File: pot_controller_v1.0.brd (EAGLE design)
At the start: 91.1 x 63.2 mm, 30 parts, among them IC10 4051D, IC11 4051D, IC13 4051D, IC2 4051D, IC3 4520D, IC4 4051D, IC5 4051D, IC6 4051D, IC7 4051D, IC8 4051D

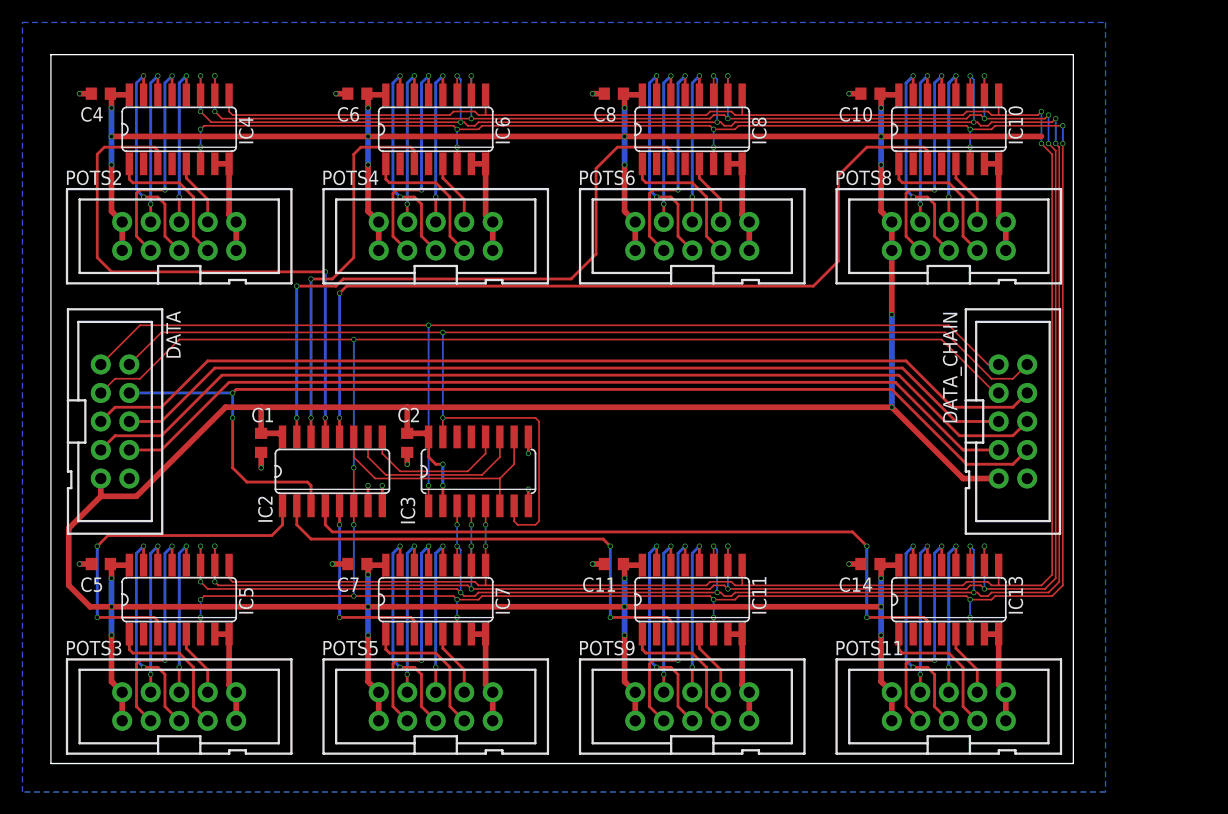
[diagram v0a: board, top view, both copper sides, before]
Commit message: Fixed routing except for possible inhibit-removal
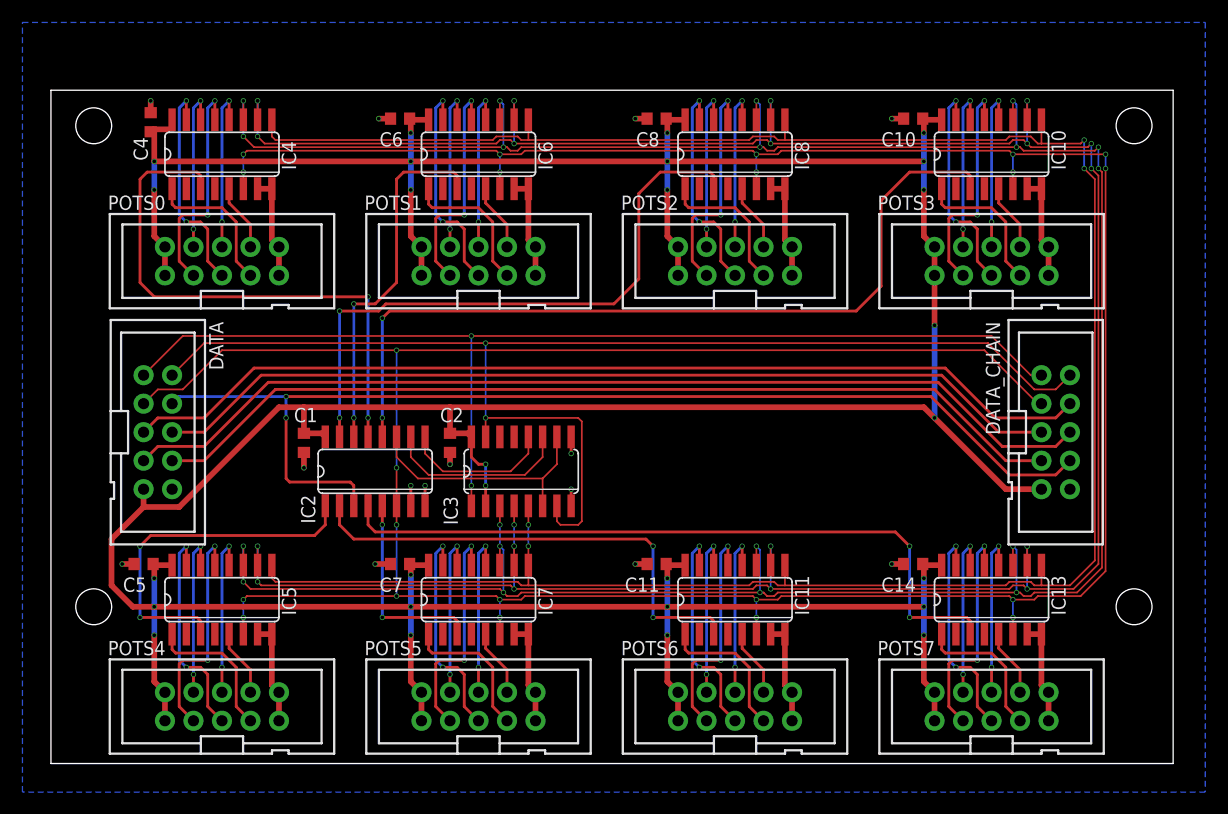
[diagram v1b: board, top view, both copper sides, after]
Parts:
- removed POTS11, POTS8, POTS9: CONN-IDC-10PS, joakim:CONN-IDC10P-S
- added POTS0, POTS1, POTS7: CONN-IDC-10PS, joakim:CONN-IDC10P-S
- moved POTS3 82.6 mm to (83.8, 44.8)
- moved POTS2 49.6 mm to (61.0, 44.8)
- moved POTS4 46.0 mm to (15.2, 5.08)
- moved POTS6 42.1 mm to (61.0, 5.08)
- moved C4 5.12 mm to (8.89, 57.1), turned to 90 degrees
- moved IC6 4.41 mm to (38.1, 54.3)
- moved IC8 4.41 mm to (61.0, 54.3)
- moved IC4 4.41 mm to (15.2, 54.3)
- moved C8 4.41 mm to (54.0, 57.5)
- moved C6 4.41 mm to (31.1, 57.5)
- moved IC10 4.41 mm to (83.8, 54.3)
- moved C10 4.41 mm to (76.8, 57.5)
- moved DATA_CHAIN 3.93 mm to (89.5, 29.5)
- moved DATA 3.93 mm to (9.53, 29.5)
- moved C11 3.81 mm to (54.0, 17.8)
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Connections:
- net +5V: now also POTS0.1, POTS0.2, POTS1.1, POTS1.2, POTS7.1, POTS7.2; no longer POTS11.1, POTS11.2, POTS8.1, POTS8.2, POTS9.1, POTS9.2
- net GND: now also POTS0.10, POTS0.9, POTS1.10, POTS1.9, POTS7.10, POTS7.9; no longer POTS11.10, POTS11.9, POTS8.10, POTS8.9, POTS9.10, POTS9.9
- net POT0: now also POTS0.3; no longer POTS2.3
- net POT1: now also POTS0.4; no longer POTS2.4
- net POT10: now also POTS1.7; no longer POTS4.7
- net POT11: now also POTS1.8; no longer POTS4.8
- net POT12: now also POTS2.3; no longer POTS6.3
- net POT13: now also POTS2.4; no longer POTS6.4
- net POT14: now also POTS2.5; no longer POTS6.5
- net POT15: now also POTS2.6; no longer POTS6.6
- net POT16: now also POTS2.7; no longer POTS6.7
- net POT17: now also POTS2.8; no longer POTS6.8
- net POT18: now also POTS3.3; no longer POTS8.3
- net POT19: now also POTS3.4; no longer POTS8.4
- net POT2: now also POTS0.5; no longer POTS2.5
- net POT20: now also POTS3.5; no longer POTS8.5
- net POT21: now also POTS3.6; no longer POTS8.6
- net POT22: now also POTS3.7; no longer POTS8.7
- net POT23: now also POTS3.8; no longer POTS8.8
- net POT24: now also POTS4.3; no longer POTS3.3
- net POT25: now also POTS4.4; no longer POTS3.4
- net POT26: now also POTS4.5; no longer POTS3.5
- net POT27: now also POTS4.6; no longer POTS3.6
- net POT28: now also POTS4.7; no longer POTS3.7
- net POT29: now also POTS4.8; no longer POTS3.8
- net POT3: now also POTS0.6; no longer POTS2.6
- net POT36: now also POTS6.3; no longer POTS9.3
- net POT37: now also POTS6.4; no longer POTS9.4
- net POT38: now also POTS6.5; no longer POTS9.5
- net POT39: now also POTS6.6; no longer POTS9.6
- net POT4: now also POTS0.7; no longer POTS2.7
- net POT40: now also POTS6.7; no longer POTS9.7
- net POT41: now also POTS6.8; no longer POTS9.8
- net POT42: now also POTS7.3; no longer POTS11.3
- net POT43: now also POTS7.4; no longer POTS11.4
- net POT44: now also POTS7.5; no longer POTS11.5
- net POT45: now also POTS7.6; no longer POTS11.6
- net POT46: now also POTS7.7; no longer POTS11.7
- net POT47: now also POTS7.8; no longer POTS11.8
- net POT5: now also POTS0.8; no longer POTS2.8
- net POT6: now also POTS1.3; no longer POTS4.3
- net POT7: now also POTS1.4; no longer POTS4.4
- net POT8: now also POTS1.5; no longer POTS4.5
- net POT9: now also POTS1.6; no longer POTS4.6
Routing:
- net +5V: track 412.7 -> 397.2 mm, vias 28 -> 27
- net POT_INH: track 328.3 -> 323.9 mm
- net POT_A: track 246.0 -> 242.6 mm
- net POT_B: track 239.2 -> 236.3 mm
- net POT_C: track 208.4 -> 205.6 mm
- net ROW2: track 57.7 -> 55.4 mm
- net ROW3: track 76.3 -> 74.1 mm
- net ROW1: track 34.8 -> 32.6 mm
- net ROW0: track 51.7 -> 49.5 mm
- net CLK: track 99.0 -> 98.0 mm
- net RESET: track 114.2 -> 113.2 mm
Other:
- board size 91.1 x 63.2 mm -> 100 x 60 mm

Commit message: Added silk screen
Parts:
- added U$1: (no value), joakim:XONIK_LOGO_60
- renumbered DATA_CHAIN to CHAIN
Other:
- board text added: "+V"
- board text added: "0"
- board text added: "1"
- board text added: "2"
- board text added: "3"
- board text added: "4"
- board text added: "48ch potentiometer scanner v1.0"
- board text added: "4VOB"
- board text added: "5"
- board text added: "CLK"
- board text added: "G"
- board text added: "GND"
- board text added: "O1"
- board text added: "O2"
- board text added: "O3"
- board text added: "O4"
- board text added: "O5"
- board text added: "RST"
- board text added: "V+"

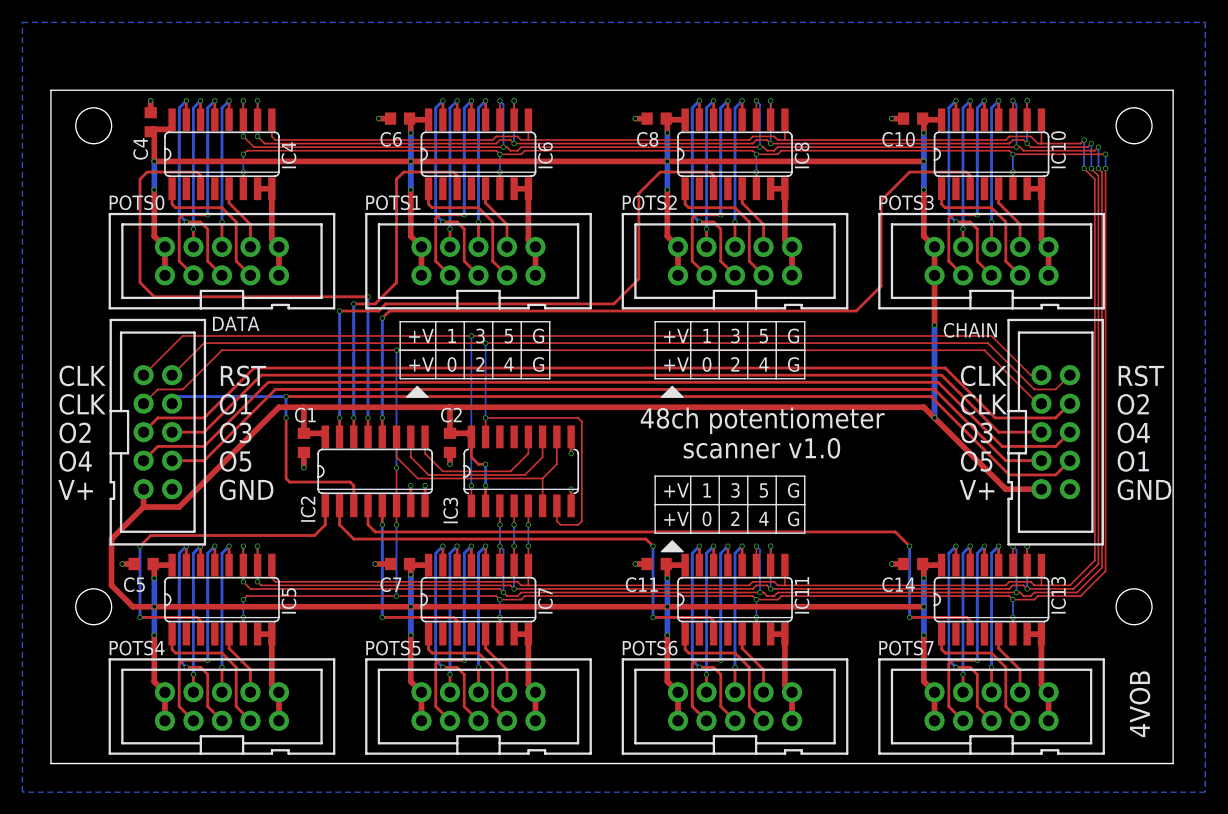
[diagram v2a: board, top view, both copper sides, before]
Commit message: Updated IDC connector
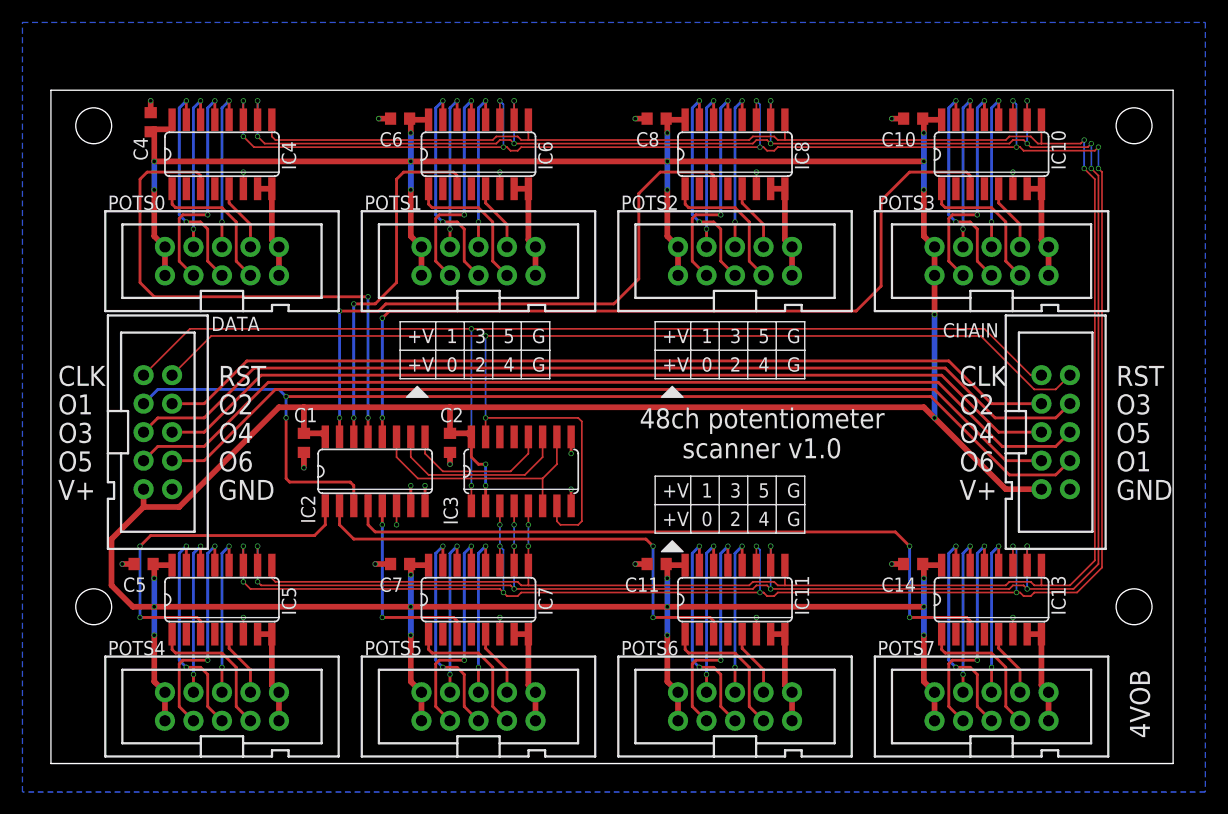
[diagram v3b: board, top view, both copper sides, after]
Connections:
- removed net POT_INH: CHAIN.3, DATA.3, IC10.6, IC11.6, IC13.6, IC2.6, IC4.6, IC5.6, IC6.6, IC7.6, IC8.6
- new net POT_VAL_CHAIN_5: CHAIN.7, DATA.8
- net GND: now also IC10.6, IC11.6, IC13.6, IC2.6, IC4.6, IC5.6, IC6.6, IC7.6, IC8.6
- net POT_VALUE: now also DATA.3; no longer DATA.4
- net POT_VAL_CHAIN_1: now also CHAIN.3, DATA.4; no longer CHAIN.4, DATA.5
- net POT_VAL_CHAIN_2: now also CHAIN.4, DATA.5; no longer CHAIN.5, DATA.6
- net POT_VAL_CHAIN_3: now also CHAIN.5, DATA.6; no longer CHAIN.6, DATA.7
- net POT_VAL_CHAIN_4: now also CHAIN.6, DATA.7; no longer CHAIN.7, DATA.8
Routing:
- net POT_INH: track 323.9 -> 0.00 mm, vias 22 -> 0
- net POT_VAL_CHAIN_5: track 0.00 -> 82.7 mm
- net GND: track 91.8 -> 105.4 mm, vias 14 -> 23
- net POT_VAL_CHAIN_3: track 88.3 -> 81.7 mm
- net POT_VAL_CHAIN_1: track 87.3 -> 80.6 mm
- net POT_VAL_CHAIN_2: track 81.7 -> 87.3 mm
- net POT_VAL_CHAIN_4: track 82.7 -> 88.3 mm
- net POT_VALUE: track 99.1 -> 102.2 mm
- net CLK: track 98.0 -> 99.2 mm
- net RESET: track 113.2 -> 114.4 mm
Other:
- board text added: "O6"
